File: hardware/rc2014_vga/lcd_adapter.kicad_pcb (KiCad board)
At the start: 2 copper layers, 24 parts, among them J1 CMOD-A7, J2 Conn_01x02_Male, J3 Conn_02x14_Odd_Even, J4 DB15_Female, J5 Conn_01x33, J6 Conn_02x17_Odd_Even, U1 SN74LVCC4245A, U2 SN74LVCC4245A, U3 SN74LVCC4245A

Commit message: working on layout
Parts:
- removed J3: Conn_02x14_Odd_Even, Connector_PinHeader_2.54mm:PinHeader_2x14_P2.54mm_Vertical
- added C1: 0.1uF, Capacitor_SMD:C_1206_3216Metric_Pad1.33x1.80mm_HandSolder, F.Cu at (165.1, 30.5)
- added C2: 0.1uF, Capacitor_SMD:C_1206_3216Metric_Pad1.33x1.80mm_HandSolder, F.Cu at (244.5, 57.8)
- added C3: 0.1uF, Capacitor_SMD:C_1206_3216Metric_Pad1.33x1.80mm_HandSolder, F.Cu at (234.3, 57.8)
- added C4: 0.1uF, Capacitor_SMD:C_1206_3216Metric_Pad1.33x1.80mm_HandSolder, F.Cu at (180.3, 30.5)
- added C5: 0.1uF, Capacitor_SMD:C_1206_3216Metric_Pad1.33x1.80mm_HandSolder, F.Cu at (194.0, 60.3)
- added C6: 1uF, Capacitor_SMD:C_1206_3216Metric_Pad1.33x1.80mm_HandSolder, F.Cu at (168.9, 59.0)
- added C7: 0.1uF, Capacitor_SMD:C_1206_3216Metric_Pad1.33x1.80mm_HandSolder, F.Cu at (168.9, 62.3)
- added C8: 1uF, Capacitor_SMD:C_1206_3216Metric_Pad1.33x1.80mm_HandSolder, F.Cu at (174.9, 59.0)
- added J7: Conn_01x06_Male, Connector_PinHeader_2.54mm:PinHeader_1x06_P2.54mm_Vertical, F.Cu at (154.9, 47.0)
- added J8: Mini-DIN-6, Connector_PinSocket_2.54mm:PinSocket_2x03_P2.54mm_Vertical, F.Cu at (157.5, 36.8)
- added JP2: Jumper_3_Bridged12, Connector_PinSocket_2.54mm:PinSocket_1x03_P2.54mm_Vertical, F.Cu at (221.0, 61.0)
- added JP3: Jumper_3_Bridged12, Connector_PinSocket_2.54mm:PinSocket_1x03_P2.54mm_Vertical, F.Cu at (210.2, 61.0)
- added U4: SN74LV1T34DBV, Package_TO_SOT_SMD:SOT-23-5, F.Cu at (186.7, 30.5)
- added U5: LTC1844ES5-3.3, Package_TO_SOT_SMD:SOT-23-5_HandSoldering, F.Cu at (182.9, 60.3)
- added X1: 100.00MHz, Package_TO_SOT_SMD:SOT-23-5_HandSoldering, F.Cu at (201.3, 60.3)
- J6: value Conn_02x17_Odd_Even -> RC2014_BUS; footprint Connector_PinHeader_2.54mm:PinHeader_2x17_P2.54mm_Vertical -> myRC2014_footprints:RC2014_Header
- R1, R10, R11, R12, R13, R14, R2, R3, R4, R5, R6, R7, R8, R9: footprint Resistor_THT:R_Axial_DIN0309_L9.0mm_D3.2mm_P12.70mm_Horizontal -> Resistor_SMD:R_1206_3216Metric_Pad1.30x1.75mm_HandSolder
- U1, U2, U3: value SN74LVCC4245A -> SN74LV1T34DBV; footprint Package_SO:SO-24_5.3x15mm_P1.27mm -> Package_TO_SOT_SMD:SOT-23-5
- moved R7 190.0 mm to (240.7, 30.5), turned to 90 degrees
- moved R10 189.5 mm to (229.9, 24.1), turned to 90 degrees
- moved R8 183.8 mm to (237.5, 30.5), turned to 90 degrees
- moved R2 182.4 mm to (243.8, 24.1), turned to 90 degrees
- moved R1 175.0 mm to (247.0, 24.1), turned to 90 degrees
- moved R9 168.5 mm to (233.0, 24.1), turned to 90 degrees
- moved R12 151.4 mm to (223.5, 24.1), turned to 90 degrees
- moved R4 144.8 mm to (237.5, 24.1), turned to 90 degrees
- moved R13 142.3 mm to (229.9, 30.5), turned to 90 degrees
- moved J5 138.9 mm to (212.1, 26.7), turned to 180 degrees
- moved R5 130.5 mm to (247.0, 30.5), turned to 90 degrees
- moved J4 128.3 mm to (238.8, 39.4), turned to 90 degrees
- moved R6 127.6 mm to (243.8, 30.5), turned to 90 degrees
- moved R3 125.3 mm to (240.7, 24.1), turned to 90 degrees
- moved R11 121.7 mm to (226.7, 24.1), turned to 90 degrees
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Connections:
- J1 pad 1: /D0 -> Net-(J1-Pad1)
- J1 pad 18: /A7 -> Net-(J1-Pad18)
- J1 pad 19: /A8 -> Net-(J1-Pad19)
- J1 pad 20: /A9 -> Net-(J1-Pad20)
- J1 pad 21: /A10 -> Net-(J1-Pad21)
- J1 pad 22: /A11 -> /KB_CLOCK
- J1 pad 23: /READ -> /KB_DATA
- J1 pad 25: GND -> +3V3
- J1 pad 26: /WRITE -> /LCD_CLK
- J1 pad 27: /LCD_DEN -> /LCD_HS
- J1 pad 28: /LCD_B5 -> /LCD_VS
- J1 pad 29: /LCD_B4 -> /LCD_R0
- J1 pad 30: /LCD_B3 -> /LCD_R1
- J1 pad 31: /LCD_B2 -> /LCD_R2
- J1 pad 32: /LCD_B1 -> /LCD_R3
- J1 pad 33: /LCD_B0 -> /LCD_R4
- J1 pad 34: /LCD_G5 -> /LCD_R5
- J1 pad 35: /LCD_G4 -> /LCD_G0
- J1 pad 36: /LCD_G3 -> /LCD_G1
- J1 pad 38: /LCD_G1 -> /LCD_G3
- J1 pad 39: /LCD_G0 -> /LCD_G4
- J1 pad 40: /LCD_R5 -> /LCD_G5
- J1 pad 41: /LCD_R4 -> /LCD_B0
- J1 pad 42: /LCD_R3 -> /LCD_B1
- J1 pad 43: /LCD_R2 -> /LCD_B2
- J1 pad 44: /LCD_R1 -> /LCD_B3
- J1 pad 45: /LCD_R0 -> /LCD_B4
- J1 pad 46: /LCD_VS -> /LCD_B5
- J1 pad 47: /LCD_HS -> /LCD_DEN
- J1 pad 48: /LCD_CLK -> Net-(J1-Pad48)
- J1 pad 8: /D7 -> Net-(J1-Pad8)
- J1 pad 9: /A0 -> Net-(J1-Pad9)
- J2 pad 1: GND -> +3V3
- J2 pad 2: GND -> +3V3
- J4 pad 10: GND -> +3V3
- J4 pad 5: GND -> +3V3
- J4 pad 6: GND -> +3V3
- J4 pad 7: GND -> +3V3
- J4 pad 8: GND -> +3V3
- J5 pad 1: GND -> +3V3
- J5 pad 12: GND -> +3V3
- J5 pad 19: GND -> +3V3
- J5 pad 26: GND -> +3V3
- J5 pad 31: GND -> +3V3
- J5 pad 33: GND -> +3V3
- J5 pad 5: GND -> +3V3
- J6 pad 1: +5V -> Net-(J6-Pad1)
- J6 pad 17: Net-(J6-Pad17) -> +3V3
- J6 pad 18: Net-(J6-Pad18) -> +5V
- J6 pad 2: +5V -> Net-(J6-Pad2)
- J6 pad 23: GND -> Net-(J6-Pad23)
- J6 pad 24: GND -> Net-(J6-Pad24)
- J6 pad 3: +5V -> Net-(J6-Pad3)
- J6 pad 33: GND -> Net-(J6-Pad33)
- J6 pad 34: GND -> Net-(J6-Pad34)
- J6 pad 4: +5V -> Net-(J6-Pad4)
- J6 pad 5: GND -> Net-(J6-Pad5)
- J6 pad 6: GND -> Net-(J6-Pad6)
- J6 pad 7: /DIR -> Net-(J6-Pad7)
- J6 pad 9: /~OE -> Net-(J6-Pad9)
- JP1 pad 1: GND -> +3V3
- R1 pad 2: /VGA_R0 -> /LCD_R0
- R10 pad 2: /VGA_B1 -> /LCD_B1
- R11 pad 2: /VGA_B2 -> /LCD_B2
- R12 pad 2: /VGA_B3 -> /LCD_B3
- R13 pad 2: /VGA_HS -> /LCD_HS
- R14 pad 2: /VGA_VS -> /LCD_VS
- R2 pad 2: /VGA_R1 -> /LCD_R1
- R3 pad 2: /VGA_R2 -> /LCD_R2
- R4 pad 2: /VGA_R3 -> /LCD_R3
- R5 pad 2: /VGA_G0 -> /LCD_G0
- R6 pad 2: /VGA_G1 -> /LCD_G1
- R7 pad 2: /VGA_G2 -> /LCD_G2
- R8 pad 2: /VGA_G3 -> /LCD_G3
- R9 pad 2: /VGA_B0 -> /LCD_B0
- U1 pad 1: +5V -> Net-(U1-Pad1)
- U1 pad 2: /DIR -> Net-(J1-Pad1)
- U1 pad 3: Net-(J6-Pad8) -> +3V3
- U1 pad 4: Net-(J6-Pad10) -> Net-(JP2-Pad2)
- U1 pad 5: Net-(J6-Pad12) -> +5V
- U2 pad 1: +5V -> Net-(U2-Pad1)
- U2 pad 2: +5V -> Net-(JP3-Pad2)
- U2 pad 3: Net-(J6-Pad26) -> +3V3
- U2 pad 4: Net-(J6-Pad28) -> Net-(J1-Pad2)
- U2 pad 5: Net-(J6-Pad30) -> +3V3
- U3 pad 1: +5V -> Net-(U3-Pad1)
- U3 pad 2: +5V -> /PS2-CLK
- U3 pad 3: Net-(J6-Pad21) -> +3V3
- U3 pad 4: Net-(J6-Pad19) -> /KB_CLOCK
- U3 pad 5: Net-(J6-Pad17) -> +3V3
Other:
- board outline added: 99.1 x 49.9 mm

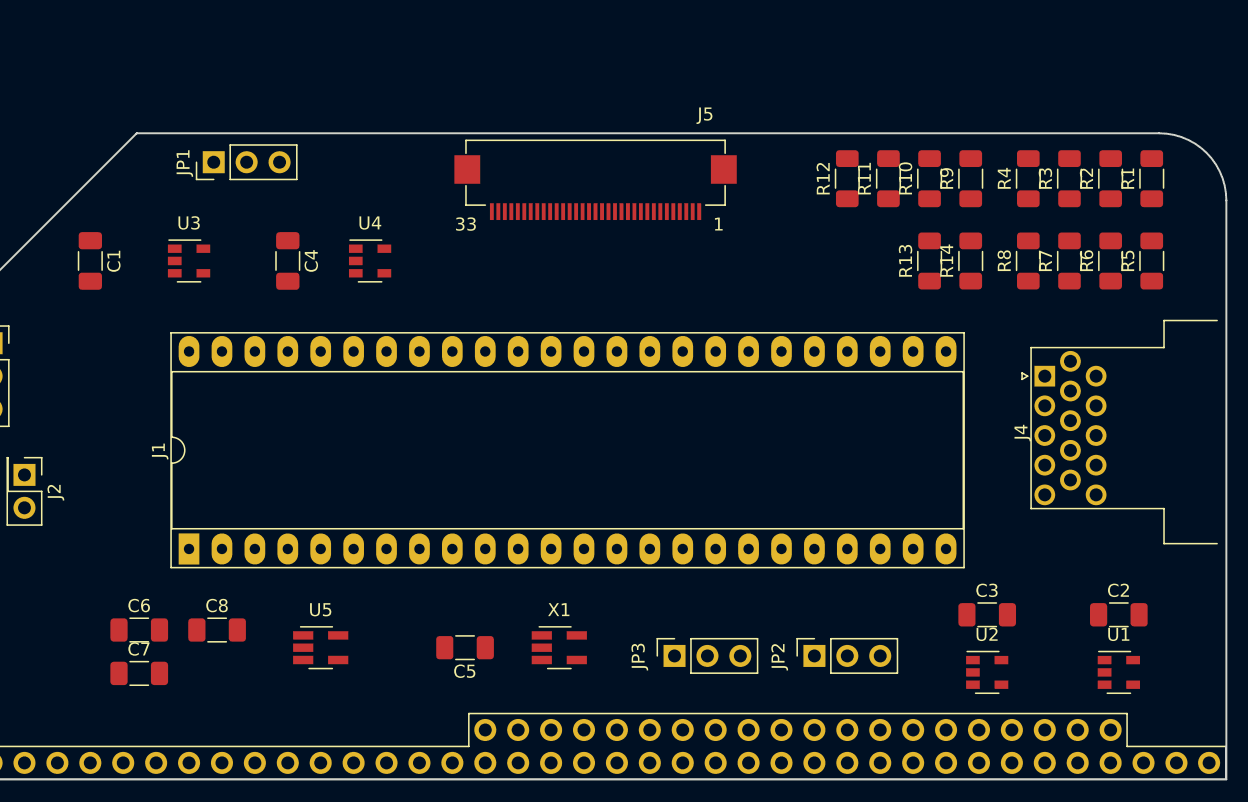
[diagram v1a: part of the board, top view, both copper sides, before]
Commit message: Change all to TH
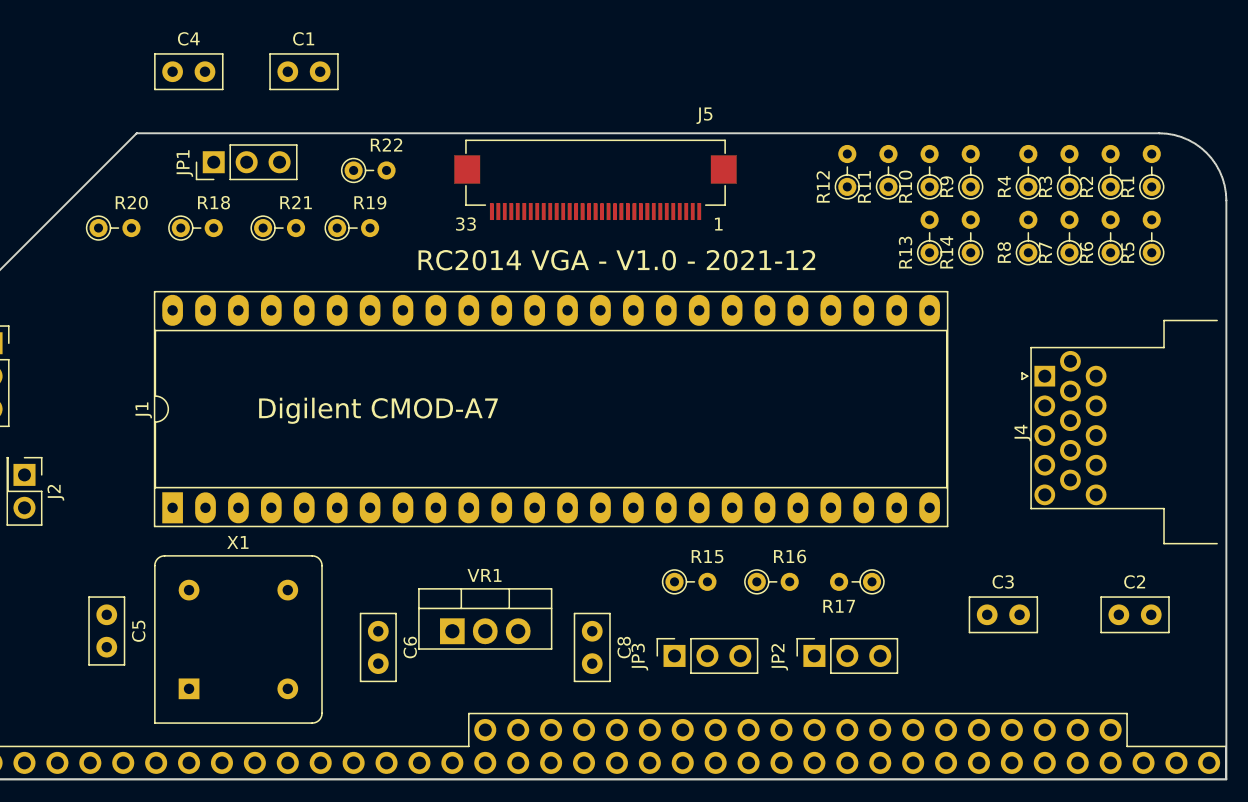
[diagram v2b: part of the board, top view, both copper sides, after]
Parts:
- removed C7: 0.1uF, Capacitor_SMD:C_1206_3216Metric_Pad1.33x1.80mm_HandSolder
- removed U1, U2, U3, U4: SN74LV1T34DBV, Package_TO_SOT_SMD:SOT-23-5
- removed U5: LTC1844ES5-3.3, Package_TO_SOT_SMD:SOT-23-5_HandSoldering
- added R15: 2k, Resistor_THT:R_Axial_DIN0204_L3.6mm_D1.6mm_P2.54mm_Vertical, F.Cu at (210.2, 55.2)
- added R16: 2k, Resistor_THT:R_Axial_DIN0204_L3.6mm_D1.6mm_P2.54mm_Vertical, F.Cu at (216.5, 55.2)
- added R17: 3k, Resistor_THT:R_Axial_DIN0204_L3.6mm_D1.6mm_P2.54mm_Vertical, F.Cu at (225.4, 55.2)
- added R18: 2k, Resistor_THT:R_Axial_DIN0204_L3.6mm_D1.6mm_P2.54mm_Vertical, F.Cu at (172.1, 27.9)
- added R19: 2k, Resistor_THT:R_Axial_DIN0204_L3.6mm_D1.6mm_P2.54mm_Vertical, F.Cu at (184.2, 27.9)
- added R20: 3k, Resistor_THT:R_Axial_DIN0204_L3.6mm_D1.6mm_P2.54mm_Vertical, F.Cu at (165.7, 27.9)
- added R21: 3k, Resistor_THT:R_Axial_DIN0204_L3.6mm_D1.6mm_P2.54mm_Vertical, F.Cu at (178.4, 27.9)
- added R22: 2k, Resistor_THT:R_Axial_DIN0204_L3.6mm_D1.6mm_P2.54mm_Vertical, F.Cu at (185.4, 23.5)
- added VR1: LM2937xT, Package_TO_SOT_THT:TO-220-3_Vertical, F.Cu at (193.0, 59.1)
- C1, C2, C3, C4, C5: footprint Capacitor_SMD:C_1206_3216Metric_Pad1.33x1.80mm_HandSolder -> Capacitor_THT:C_Disc_D5.0mm_W2.5mm_P2.50mm
- C6: value 1uF -> 0.1uF; footprint Capacitor_SMD:C_1206_3216Metric_Pad1.33x1.80mm_HandSolder -> Capacitor_THT:C_Disc_D5.0mm_W2.5mm_P2.50mm
- C8: value 1uF -> 10uF; footprint Capacitor_SMD:C_1206_3216Metric_Pad1.33x1.80mm_HandSolder -> Capacitor_THT:C_Disc_D5.0mm_W2.5mm_P2.50mm
- R1, R10, R11, R12, R13, R14, R2, R3, R4, R5, R6, R7, R8, R9: footprint Resistor_SMD:R_1206_3216Metric_Pad1.30x1.75mm_HandSolder -> Resistor_THT:R_Axial_DIN0204_L3.6mm_D1.6mm_P2.54mm_Vertical
- X1: value 100.00MHz -> CXO_DIP8; footprint Package_TO_SOT_SMD:SOT-23-5_HandSoldering -> Oscillator:Oscillator_DIP-8
- moved C8 29.0 mm to (203.8, 59.1), turned to 270 degrees
- moved X1 28.8 mm to (172.7, 63.5)
- moved C5 27.8 mm to (166.4, 57.8), turned to 270 degrees
- moved C1 21.1 mm to (180.3, 15.9), turned to 0 degrees
- moved C6 18.5 mm to (187.3, 59.1), turned to 270 degrees
- moved C4 17.1 mm to (171.4, 15.9), turned to 0 degrees
- moved J1 3.42 mm to (171.4, 49.5)
- moved R1 0.64 mm to (247.0, 24.8)
- moved R10 0.64 mm to (229.9, 24.8)
- moved R11 0.64 mm to (226.7, 24.8)
- moved R12 0.64 mm to (223.5, 24.8)
- moved R13 0.64 mm to (229.9, 29.8)
- moved R14 0.64 mm to (233.0, 29.8)
- moved R2 0.64 mm to (243.8, 24.8)
- moved R3 0.64 mm to (240.7, 24.8)
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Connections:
- C1 pad 2: +3V3 -> GND
- C2 pad 2: +3V3 -> GND
- C3 pad 2: +3V3 -> GND
- C4 pad 2: +3V3 -> GND
- C5 pad 2: +3V3 -> GND
- C6 pad 2: +3V3 -> GND
- C8 pad 2: +3V3 -> GND
- J1 pad 25: +3V3 -> GND
- J2 pad 1: +3V3 -> GND
- J2 pad 2: +3V3 -> GND
- J4 pad 10: +3V3 -> GND
- J4 pad 5: +3V3 -> GND
- J4 pad 6: +3V3 -> GND
- J4 pad 7: +3V3 -> GND
- J4 pad 8: +3V3 -> GND
- J5 pad 1: +3V3 -> GND
- J5 pad 12: +3V3 -> GND
- J5 pad 19: +3V3 -> GND
- J5 pad 26: +3V3 -> GND
- J5 pad 31: +3V3 -> GND
- J5 pad 32: +3V3 -> /LCD_DISP
- J5 pad 33: +3V3 -> GND
- J5 pad 5: +3V3 -> GND
- J6 pad 17: +3V3 -> GND
- J6 pad B1: +3V3 -> GND
- J7 pad 1: +3V3 -> GND
- J7 pad 2: +3V3 -> GND
- J8 pad 3: +3V3 -> GND
- JP1 pad 1: +3V3 -> GND
- X1 pad 1: +3V3 -> Net-(X1-Pad1)
- X1 pad 4: +3V3 -> GND
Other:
- board text added: "Digilent CMOD-A7"
- board text added: "RC2014 VGA - V1.0 - 2021-12"

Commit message: working on layout
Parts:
- removed J5: Conn_01x33, lcd_adapter:FH12-33S-0.5
- added J3: Conn_01x34, Connector_PinHeader_2.00mm:PinHeader_2x17_P2.00mm_Vertical, F.Cu at (219.1, 22.9)
- moved C3 62.5 mm to (188.0, 15.9)
- moved C4 46.4 mm to (160.7, 61.0), turned to 270 degrees
- moved R19 16.0 mm to (168.3, 29.8), turned to 180 degrees
- moved C6 14.6 mm to (201.9, 59.1), turned to 90 degrees
- moved C8 14.6 mm to (189.2, 59.1), turned to 90 degrees
- moved R22 12.5 mm to (174.6, 29.8), turned to 180 degrees
- moved J2 8.52 mm to (163.8, 54.6), turned to 0 degrees
- moved R12 5.99 mm to (226.7, 29.8)
- moved VR1 5.08 mm to (198.1, 59.1), turned to 180 degrees
- moved C5 3.22 mm to (166.4, 61.0)
- moved R21 2.84 mm to (181.0, 26.7), turned to 180 degrees
- moved R18 1.28 mm to (172.2, 26.7)
- moved R20 1.28 mm to (165.9, 26.7)
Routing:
- net +5V: track 0.00 -> 84.6 mm
- net /LCD_B1: track 0.00 -> 55.6 mm, vias 0 -> 3
- net /LCD_B0: track 0.00 -> 54.1 mm, vias 0 -> 2
- net /LCD_B2: track 0.00 -> 53.3 mm, vias 0 -> 1
- net /LCD_R3: track 0.00 -> 39.0 mm, vias 0 -> 1
- net /LCD_DEN: track 0.00 -> 28.0 mm, vias 0 -> 1
- net /LCD_B5: track 0.00 -> 27.1 mm, vias 0 -> 1
- net /LCD_B4: track 0.00 -> 25.9 mm, vias 0 -> 1
- net /LCD_B3: track 0.00 -> 24.6 mm, vias 0 -> 1
- net /LCD_G5: track 0.00 -> 20.2 mm, vias 0 -> 2
- net /LCD_G4: track 0.00 -> 19.2 mm, vias 0 -> 2
- net /LCD_G3: track 0.00 -> 15.6 mm, vias 0 -> 2
- net /LCD_G2: track 0.00 -> 14.8 mm, vias 0 -> 1
- net /LCD_G1: track 0.00 -> 14.5 mm, vias 0 -> 2
- net /LCD_CLK: track 0.00 -> 14.1 mm
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- added copper zone on F.Cu, net +3V3
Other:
- net class Default: clearance 0.2 -> 0.1778; trace_width 0.25 -> 0.1778; via_dia 0.8 -> 0.508; via_drill 0.4 -> 0.254
- rule trace_clearance: 0.2 -> 0.1778
- rule trace_min: 0.2 -> 0.1778
- rule via_min_drill: 0.3 -> 0.254
- rule via_min_size: 0.4 -> 0.508

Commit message: routing
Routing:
- net +3V3: track 0.00 -> 58.8 mm
- net /LCD_G0: track 12.5 -> 70.5 mm, vias 0 -> 2
- net /LCD_G2: track 14.8 -> 70.2 mm, vias 1 -> 3
- net /LCD_G1: track 14.5 -> 54.4 mm, vias 2 -> 4
- net /LCD_R0: track 11.3 -> 49.7 mm, vias 0 -> 2
- net /LCD_B3: track 24.6 -> 62.3 mm, vias 1 -> 2
- net /LCD_R1: track 13.1 -> 50.0 mm, vias 0 -> 1
- net Net-(J4-Pad3): track 0.00 -> 36.5 mm, vias 0 -> 2
- net /LCD_HS: track 0.00 -> 35.7 mm, vias 0 -> 1
- net /LCD_G3: track 15.6 -> 49.8 mm
- net /LCD_R2: track 10.1 -> 42.2 mm, vias 0 -> 2
- net Net-(J4-Pad14): track 0.00 -> 29.1 mm, vias 0 -> 1
- net Net-(J4-Pad13): track 0.00 -> 28.5 mm, vias 0 -> 2
- net /PS2-CLK: track 0.00 -> 26.7 mm
- net Net-(J4-Pad1): track 0.00 -> 24.7 mm
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
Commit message: As built pcb
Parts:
- removed C1, C3: 0.1uF, Capacitor_THT:C_Disc_D5.0mm_W2.5mm_P2.50mm
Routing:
- net /KB_CLOCK: track 3.81 -> 81.9 mm, vias 0 -> 1
- net /KB_DATA: track 11.5 -> 83.0 mm, vias 0 -> 1
- net Net-(J1-Pad2): track 0.00 -> 53.1 mm
- net Net-(J1-Pad1): track 0.00 -> 41.1 mm
- net /TXB: track 0.00 -> 33.5 mm
- net /TXA: track 0.00 -> 30.9 mm
- net /RXB: track 0.00 -> 27.1 mm
- net Net-(J1-Pad12): track 0.00 -> 24.7 mm, vias 0 -> 1
- net /PS2-DATA: track 12.1 -> 35.0 mm, vias 1 -> 2
- net /RXA: track 0.00 -> 22.2 mm
- net /LCD_DISP: track 0.00 -> 18.2 mm, vias 0 -> 1
- net Net-(JP2-Pad2): track 0.00 -> 16.4 mm, vias 0 -> 1
- net GND: track 10.2 -> 20.8 mm
- net Net-(JP3-Pad2): track 0.00 -> 10.4 mm
- net /LCD_B1: track 55.6 -> 61.9 mm, vias 3 -> 4
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- added copper zone on B.Cu, net GND
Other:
- board text added: "github.com/eshazen"
